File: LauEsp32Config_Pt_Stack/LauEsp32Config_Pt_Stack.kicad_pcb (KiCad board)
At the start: 4 copper layers, 55 x 45 mm, 58 parts, among them J1 DF40 Bank A (BOTTOM, plug), J2 DF40 Bank B (BOTTOM, plug), J3 DF40 Control (BOTTOM, plug), J4 DF40 Bank A (TOP, receptacle), J5 DF40 Bank B (TOP, receptacle), J6 DF40 Control (TOP, receptacle), J7 microSD Molex 104031-0811, Q1 2N7002, Q2 2N7002, U1 ESP32-S3-MINI-1U-N8, U2 SN74LVC125APWR

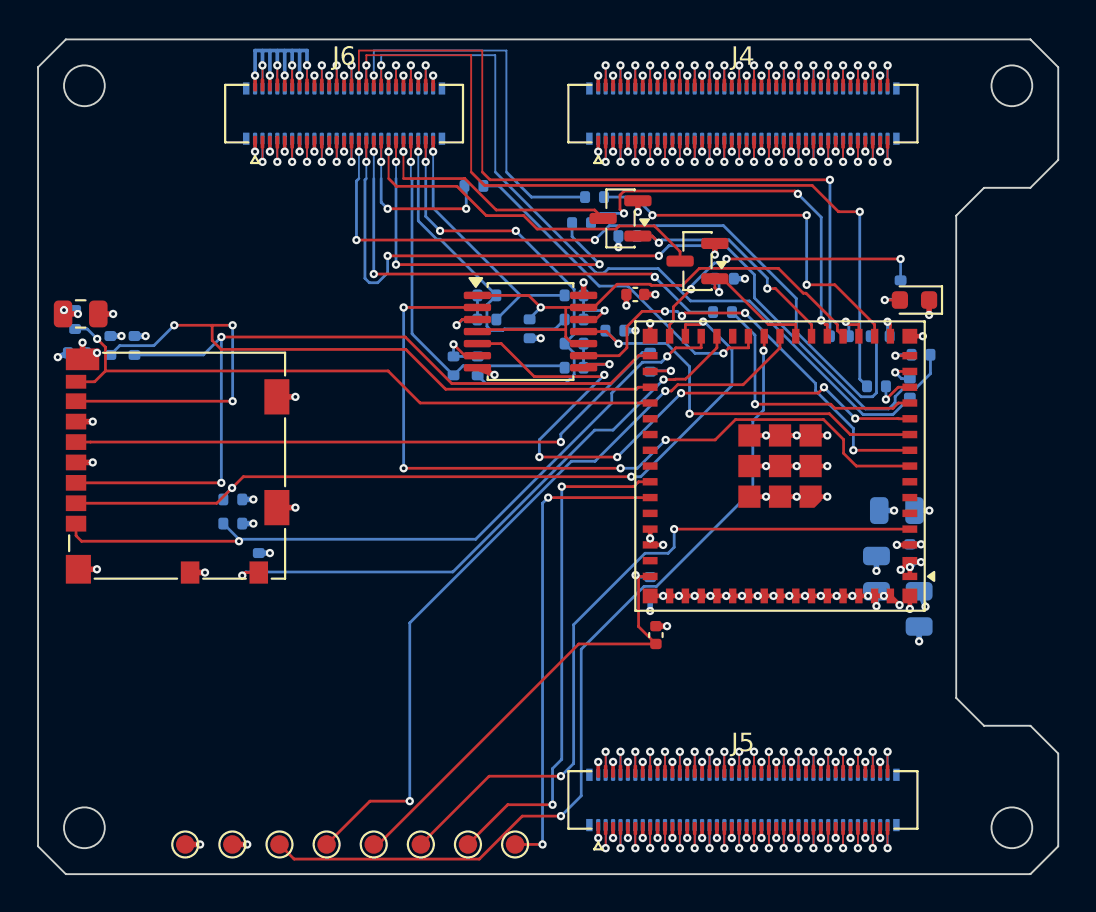
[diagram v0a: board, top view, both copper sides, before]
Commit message: feat(esp32-card): GND pours on both outer layers, thinned stitching, power-connectivity check -- DRC CLEAN
Layout review found the only ground was In1: B.Cu tracks referenced the +3V3 plane and fast
nets changed layer with no ground via beside them.

add_ground_pours.py: GND pours on F.Cu and B.Cu (0.15 mm clearance, thermal reliefs; U1 solid --
its 0.85 mm-pitch pads only fit one spoke), antenna no-pour area, GND companion vias beside
autorouted signal vias (50).

thin_stitching.py: the 2 mm stitching grid (180 vias) was overkill (lambda/20 is ~7 mm for the
80 MHz SPI, ~3 mm only where 2.4 GHz matters) and perforated the +3V3 plane. Replaced by a 5 mm
interior grid (25), a 3 mm edge row (30) and an antenna ring (5). Vias 594 -> 474.

check_power_connectivity.py: independent copper-geometry union-find proving GND and +3V3 are each
ONE conductor (pads, vias, tracks, plane and pour fills), with a negative test (all GND vias removed
in memory must split GND) -- fixed twice: SWIG identity never matched the skipped item, and a
single-track negative test became invalid once the pours existed.

Verified on the board: DRC 0 violations / 0 unconnected / 0 footprint errors; check_board_nets.py
0 wrong nets; check_power_connectivity.py PASS.

Co-Authored-By: Claude Opus 5 (1M context) <noreply@anthropic.com>
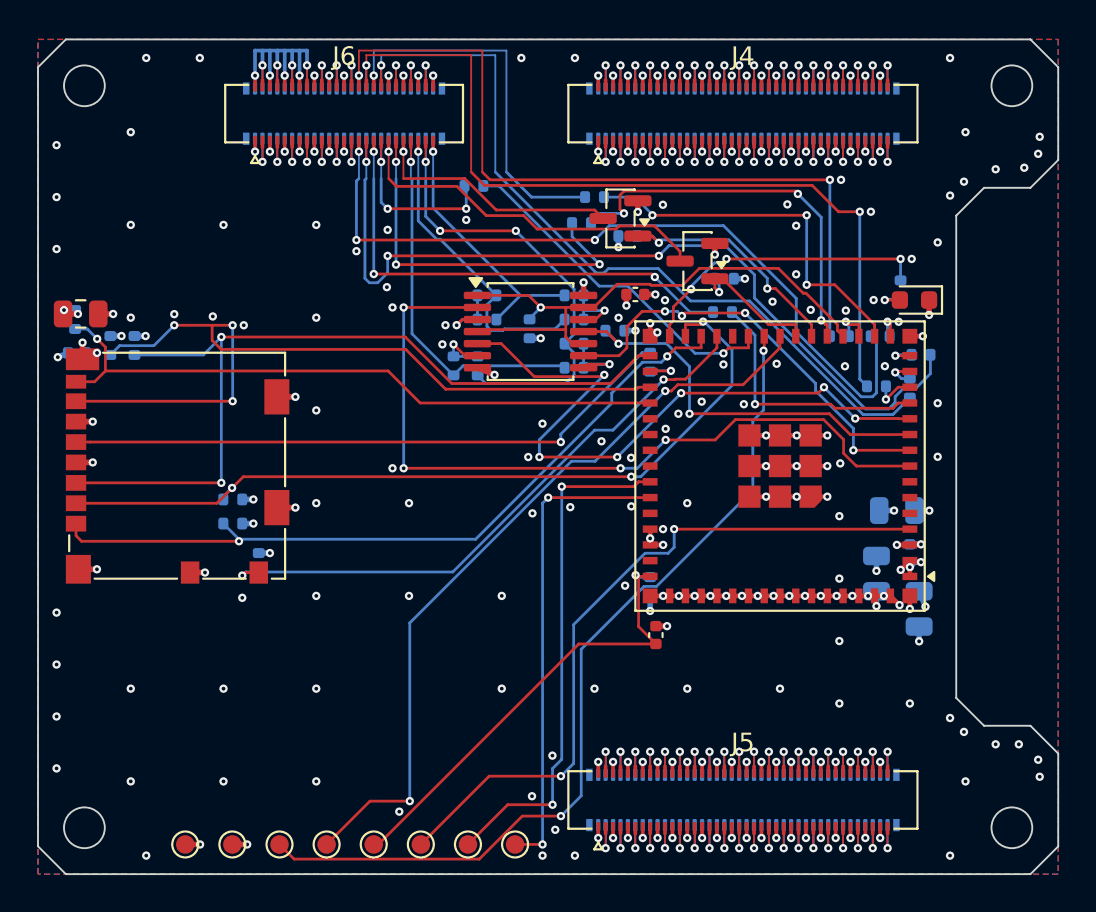
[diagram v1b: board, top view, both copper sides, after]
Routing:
- net GND: vias 122 -> 232
- added copper zone on B.Cu, net GND
- added copper zone on F.Cu, net GND

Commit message: feat(esp32-card): JTAG straps to 0R, JLCPCB upload set as ordered 2026-09-30 -- ORDERED
TCK/TMS/TDI straps R10-R12 (and rev B R14-R16) 33R -> 0R, C17168. The Pt isolates its
FT2232H with only 100R (RN2); with 33R here an ESP32 pulling low against an FTDI still
driving high (left in MPSSE by a loader run) reaches ~0.8 V at the FPGA -- VIL(max). 0R
gives ~0.3-0.4 V. TDO straps R13/R17 are received, not driven: stay 33R. Changed in
gen_schematic.py and regenerated (sch + both BOMs); the unmodified generator was first
shown to reproduce the committed files byte for byte. Board: Value and LCSC fields only.
Parity back to the 58 metadata-only MPN/LCSC warnings; DRC 0 / 0 unconnected; ERC 0.

gen_schematic.py finds KiCad under either machine's install path.

production/jlcpcb/ is exactly what was uploaded: gerbers (KiCad 10.0.3, generated twice,
identical but for timestamps, zip verified byte for byte), BOM (46 placements, 4 DNP
excluded, all 17 lines in stock), and a CPL with rotations corrected to JLC's library:
Q1/Q2 180 -> 0, U2 0 -> 270, J7 90 -> 270, found by fitting each LCSC part's EasyEDA
footprint to the KiCad one.

Pre-order review, four independent checks, no blocker: U1 land pattern and all 65 pins
vs the S3-MINI-1U datasheet; J1-J6 vs Alchitry's official V2 element library (positions,
genders, 210-pad pass-through); JTAG / PROGRAM_B / DONE / microSD / power vs the Pt Rev A
schematic; JLC DFM limits. Order: Single PCB (JLC adds rails), ENIG, 0.2 mm vias
(TG155 + Kelvin forced), Epoxy Filled & Capped for the 141 vias at or in pads.

README: status (layout routed, fab ordered), 8.1 order record, 6.0 pad table rewritten
for the S3 as built (it still described the C3), 4.2 strap-voltage note.
SCHEMATIC.md: strap values and BOM table.

Co-Authored-By: Claude Opus 5.5 <noreply@anthropic.com>
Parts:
- R10, R11, R12, R14, R15, R16: value 33R -> 0R
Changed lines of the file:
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@@
 			)
 		)
-		(property "Value" "33R"
+		(property "Value" "0R"
 			(at 0 -1.17 180)
 			(layer "B.Fab")
@@
 			)
 		)
-		(property "LCSC" "C25105"
+		(property "LCSC" "C17168"
 			(at 0 0 180)
 			(layer "B.Fab")
@@
 			)
 		)
-		(property "Value" "33R"
+		(property "Value" "0R"
 			(at 0 -1.17 270)
 			(layer "B.Fab")
@@
 			)
 		)
-		(property "LCSC" "C25105"
+		(property "LCSC" "C17168"
 			(at 0 0 270)
 			(layer "B.Fab")
@@
 			)
 		)
-		(property "Value" "33R"
+		(property "Value" "0R"
 			(at 0 -1.17 0)
 			(layer "B.Fab")
@@
 			)
 		)
-		(property "LCSC" "C25105"
+		(property "LCSC" "C17168"
 			(at 0 0 0)
 			(layer "B.Fab")
@@
 			)
 		)
-		(property "Value" "33R"
+		(property "Value" "0R"
 			(at 0 -1.17 180)
 			(layer "B.Fab")
@@
 			)
 		)
-		(property "LCSC" "C25105"
+		(property "LCSC" "C17168"
 			(at 0 0 180)
 			(layer "B.Fab")
@@
 			)
 		)
-		(property "Value" "33R"
+		(property "Value" "0R"
 			(at 0 -1.17 270)
 			(layer "B.Fab")
@@
 			)
 		)
-		(property "LCSC" "C25105"
+		(property "LCSC" "C17168"
 			(at 0 0 270)
 			(layer "B.Fab")
@@
 			)
 		)
-		(property "Value" "33R"
+		(property "Value" "0R"
 			(at 0 -1.17 0)
 			(layer "B.Fab")
@@
 			)
 		)
-		(property "LCSC" "C25105"
+		(property "LCSC" "C17168"
 			(at 0 0 0)
 			(layer "B.Fab")
